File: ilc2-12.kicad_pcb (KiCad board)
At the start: 2 copper layers, 71.1 x 40.6 mm, 7 parts, among them J1 CONN_01X22

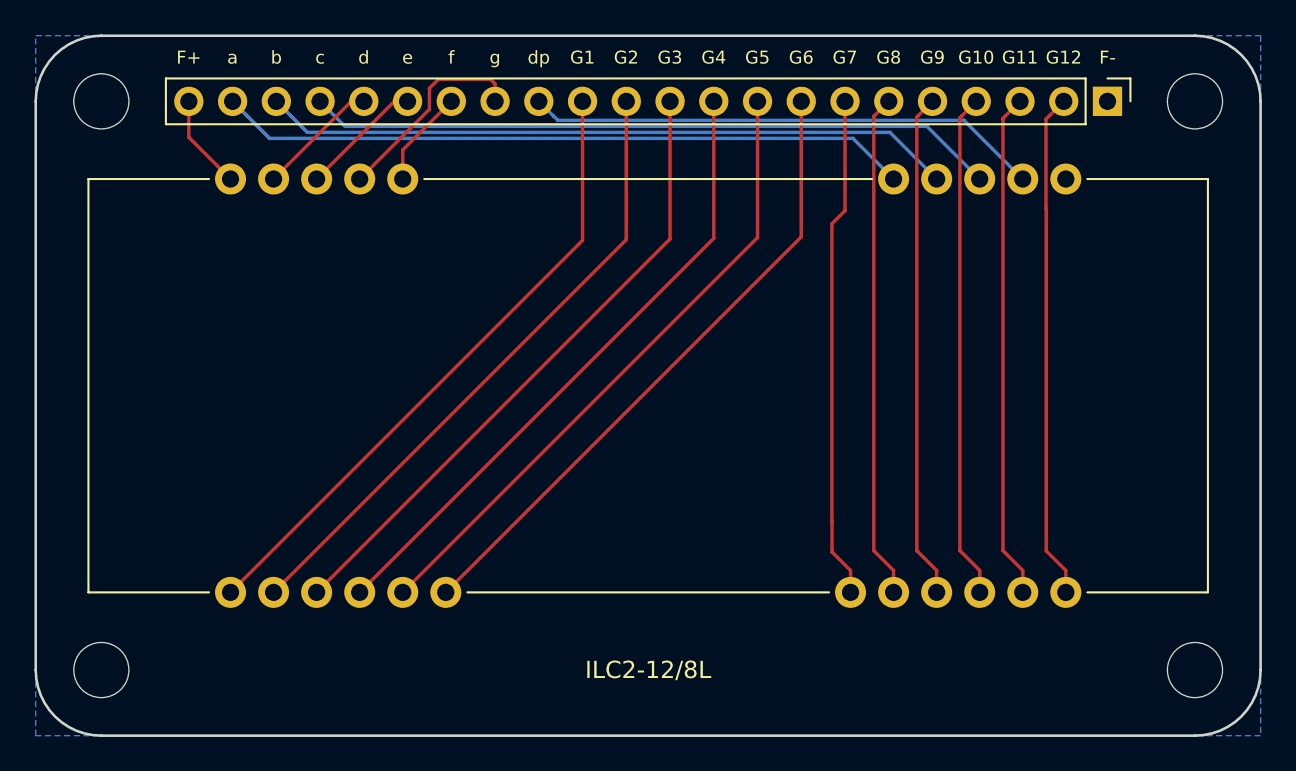
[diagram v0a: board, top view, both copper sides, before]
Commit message: Board rev 2. Fixed pin spacing
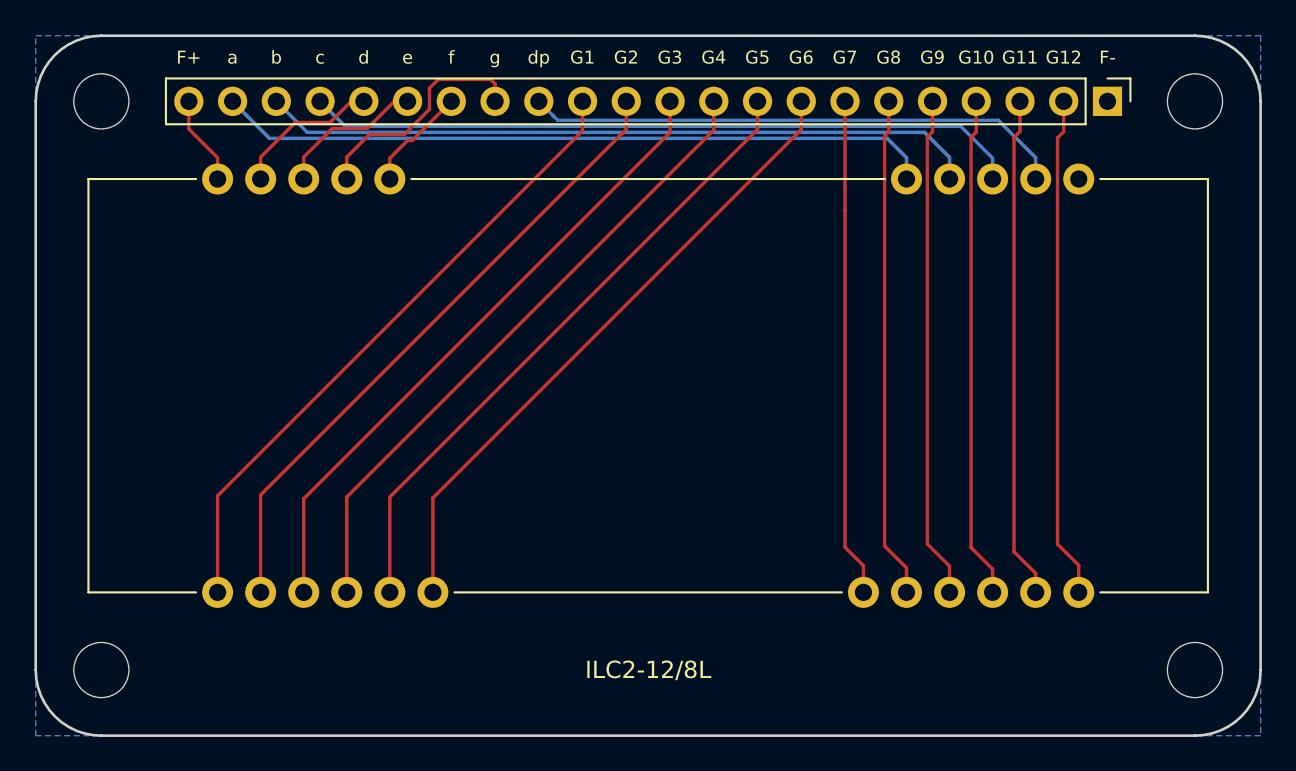
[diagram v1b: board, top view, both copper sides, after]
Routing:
- net Net-(D1-Pad2): track 7.11 -> 8.60 mm
- net Net-(D1-Pad4): track 12.1 -> 13.6 mm
- net Net-(D1-Pad3): track 7.15 -> 8.64 mm
- net Net-(D1-Pad7): track 40.2 -> 41.7 mm
- net Net-(D1-Pad9): track 30.0 -> 31.4 mm
- net Net-(D1-Pad6): track 40.2 -> 41.7 mm
- net Net-(D1-Pad8): track 40.2 -> 41.6 mm
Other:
- board text added: "https://github.com/Wiles/ilc2-12 Rev. 2"
- board text removed: "https://github.com/Wiles/ilc2-12"
